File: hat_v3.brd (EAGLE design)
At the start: 65 x 56.5 mm, 25 parts, among them U1 ADS1115IDGST, U2 ADXL345

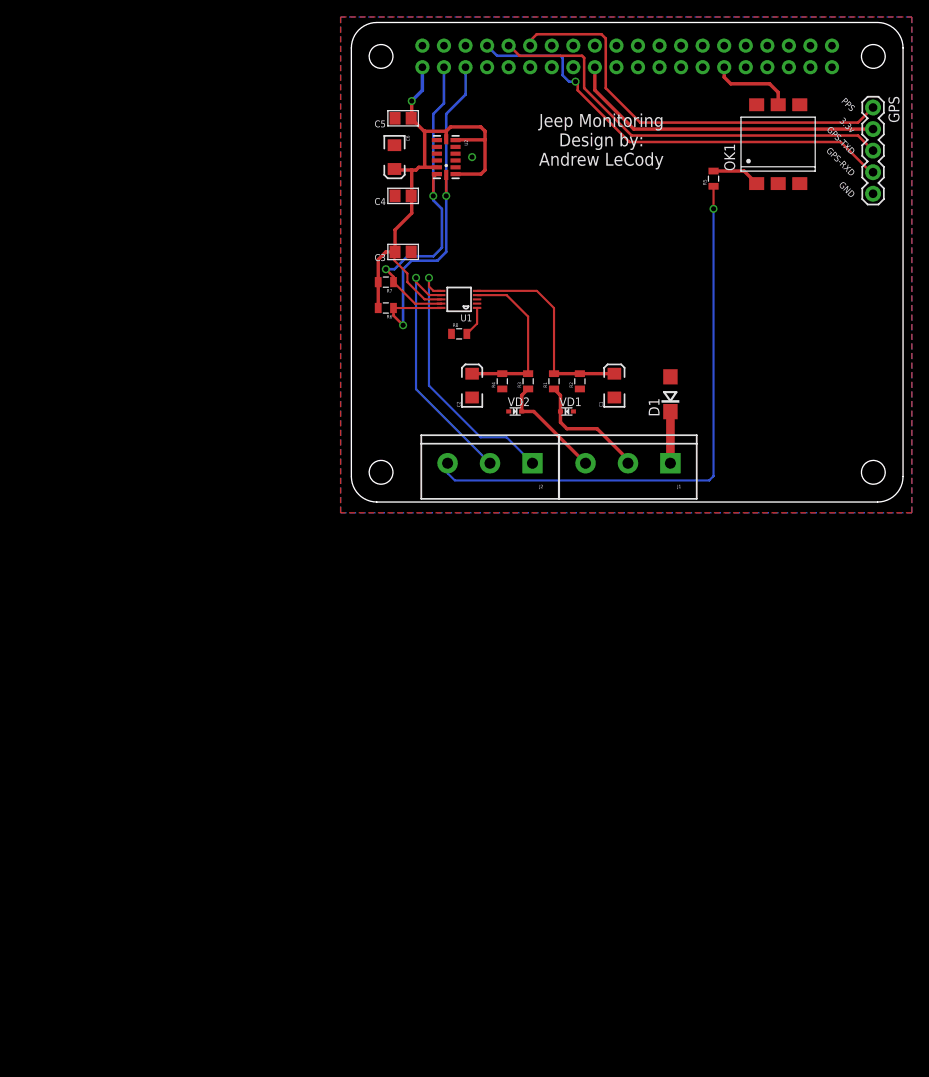
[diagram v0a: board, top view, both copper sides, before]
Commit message: V3 almost done, just need to finish MCP2515
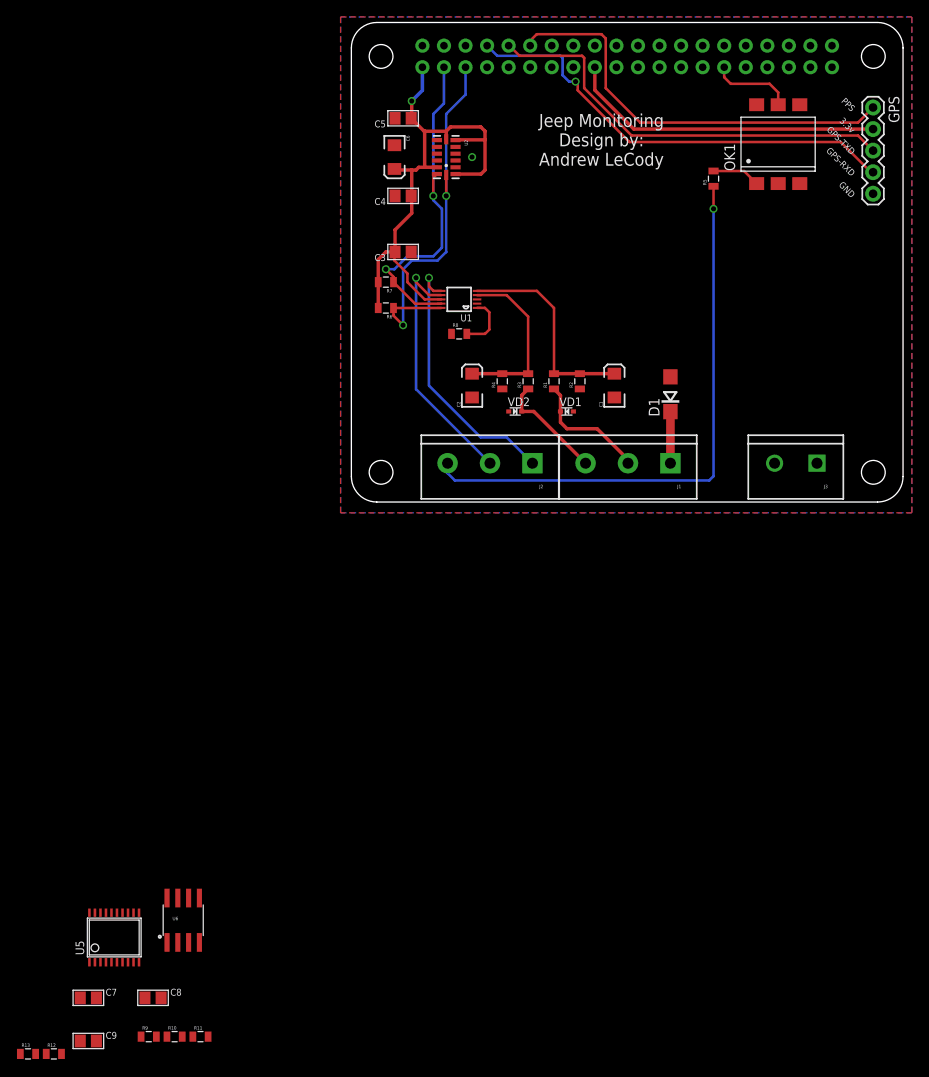
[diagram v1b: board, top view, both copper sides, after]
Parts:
- added C7, C8: 560pF, microbuilder:0805
- added C9: 0.1µF, microbuilder:0805
- added FRAME2: FRAME-LETTERNO_PACKAGE, SparkFun-Aesthetics:DUMMY
- added J3: (no value), SparkFun-Connectors:SCREWTERMINAL-5MM-2
- added R10, R11: 100, SparkFun-Passives:0805
- added R12: 10k, SparkFun-Passives:0805
- added R13: 22k, SparkFun-Passives:0805
- added R9: 4k7, SparkFun-Passives:0805
- added U5: MCP2515-I/ST, mcp2515:TSSOP20
- added U6: MCP2551, SparkFun-DigitalIC:SO08
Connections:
- removed net 5.0V: RPI1.2, RPI1.4
- new net 5V: C9.1, RPI1.2, RPI1.4, U6.2
- new net CANH: J3.1, R10.2, U6.7
- new net CANL: J3.2, R11.2, U6.6
- new net N$4: R12.1, R13.2, U5.2
- new net N$5: R9.2, U6.8
- new net N$6: C7.1, R10.1
- new net N$8: C8.1, R11.1
- new net RXCAN: R12.2, U6.4
- new net TXCAN: U5.1, U6.1
- new net VDD: U5.20
- new net VSS: U5.10
- net GND: now also C7.2, C8.2, C9.2, R13.1, R9.1, U6.3
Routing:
- net ADDR: track 3.57 -> 6.56 mm

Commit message: V3 done!
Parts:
- added C10: 100nF, microbuilder:0805
- added C11, C12: 22pF, microbuilder:0805
- added R14: 4k7, SparkFun-Passives:0805
- added X1: 16Mhz, IQD-Frequency-Products:HC49-4-HSMX
- U5: value MCP2515-I/ST -> MCP2515-I/SO; device mcp2515:TSSOP20 -> mcp2515:SO18L
- moved C9 114.0 mm to (45.7, 20.8), turned to 90 degrees
- moved R9 113.9 mm to (55.4, 18.8), turned to 270 degrees
- moved C7 112.5 mm to (54.9, 14.2)
- moved R13 107.6 mm to (27.4, 20.3), turned to 90 degrees
- moved R12 107.3 mm to (30.0, 20.3), turned to 270 degrees
- moved R10 104.2 mm to (52.8, 10.7), turned to 180 degrees
- moved C8 101.0 mm to (46.7, 14.2), turned to 180 degrees
- moved U5 99.5 mm to (24.9, 33.0), turned to 90 degrees
- moved U6 99.5 mm to (50.8, 20.8), turned to 180 degrees
- moved R11 99.3 mm to (48.8, 10.7)
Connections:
- removed net VDD: U5.20
- removed net VSS: U5.10
- new net N$14: C12.1, U5.8, X1.2
- new net N$15: C11.1, U5.7, X1.1
- new net U5_RST: R14.1, U5.17
- net 3.3V: now also C10.1, R14.2, U5.18
- net GND: now also C10.2, C11.2, C12.2, U5.9
- net GPIO25: now also U5.12
- net SPI_CE0: now also U5.16
- net SPI_MISO: now also U5.15
- net SPI_MOSI: now also U5.14
- net SPI_SCLK: now also U5.13
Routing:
- net 5V: track 0.00 -> 128.1 mm, vias 0 -> 1
- net TXCAN: track 0.00 -> 37.1 mm
- net SPI_CE0: track 0.00 -> 35.5 mm, vias 0 -> 1
- net SPI_MISO: track 0.00 -> 31.3 mm, vias 0 -> 2
- net SPI_MOSI: track 0.00 -> 29.0 mm, vias 0 -> 2
- net SPI_SCLK: track 0.00 -> 26.9 mm, vias 0 -> 1
- net GPIO25: track 0.00 -> 26.8 mm, vias 0 -> 1
- net RXCAN: track 0.00 -> 20.7 mm
- net N$15: track 0.00 -> 18.4 mm
- net CANH: track 0.00 -> 15.1 mm
- net CANL: track 0.00 -> 13.9 mm
- net 3.3V: track 103.6 -> 117.5 mm
- net N$14: track 0.00 -> 12.8 mm
- net N$4: track 0.00 -> 12.8 mm
- net N$5: track 0.00 -> 5.59 mm
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
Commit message: Reworked v3
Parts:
- removed R13: 22k, SparkFun-Passives:0805
- removed R14: 4k7, SparkFun-Passives:0805
- removed U6: MCP2551, SparkFun-DigitalIC:SO08
- added D2: (no value), diode:SOT23
- added U4: MCP2551, SparkFun-DigitalIC:SO08
- C1, C2: value 100uF -> 10uF; device SparkFun:EIA3216 -> SparkFun-Capacitors:EIA3216
- C10: value 100nF -> 0.1uF
- C6: device SparkFun:EIA3216 -> SparkFun-Capacitors:EIA3216
- R10: value 100 -> 10k
- R11: value 100 -> 22k
- R12, R7: value 10k -> 4k7
- R8: value 10k -> 100
- R9: value 4k7 -> 100
- VD1, VD2: device diode:SOD523@1 -> diode:SOD523
- moved R7 51.7 mm to (55.4, 19.3), turned to 270 degrees
- moved R8 41.1 mm to (52.8, 11.2), turned to 180 degrees
- moved R10 24.8 mm to (30.0, 20.3), turned to 270 degrees
- moved R11 23.4 mm to (27.4, 20.3), turned to 90 degrees
- moved R12 20.8 mm to (15.2, 35.1)
- moved VD1 16.8 mm to (8.64, 11.7)
- moved VD2 14.8 mm to (4.57, 11.7), turned to 0 degrees
- moved R9 10.1 mm to (48.8, 11.2), turned to 0 degrees
- moved R6 9.16 mm to (12.7, 19.8), turned to 0 degrees
- moved R1 3.56 mm to (23.9, 17.8)
- moved R3 3.56 mm to (20.8, 17.8)
- moved C3 3.41 mm to (4.57, 26.4), turned to 270 degrees
- moved C10 2.96 mm to (15.2, 30.5), turned to 270 degrees
- moved D1 1.02 mm to (37.6, 13.7)
- moved C1 0.51 mm to (31.0, 14.2)
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- renumbered U5 to U3
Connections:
- net 3.3V: now also R12.2; no longer R14.2, R6.2, R7.2
- net 5V: now also U4.2; no longer U6.2
- net ADDR: now also R6.2; no longer R8.2
- net BAT-1-INPUT: now also D2.1; no longer VD1.C
- net BAT-2-INPUT: now also D2.2; no longer VD2.C
- net CANH: now also R8.2, U4.7; no longer R10.2, U6.7
- net CANL: now also R9.2, U4.6; no longer R11.2, U6.6
- net GND: now also D2.3, R11.1, R6.1, R7.1, U4.3; no longer R13.1, R8.1, R9.1, U6.3
- net N$4: now also R10.1, R11.2; no longer R12.1, R13.2
- net N$5: now also R7.2, U4.8; no longer R9.2, U6.8
- net N$6: now also R8.1; no longer R10.1
- net N$8: now also R9.1; no longer R11.1
- net RXCAN: now also R10.2, U4.4; no longer R12.2, U6.4
- net SCL: no longer R6.1
- net SDA: no longer R7.1
- net SHUNT-HIGH-INPUT: now also VD1.C
- net SHUNT-LOW-INPUT: now also VD2.C
- net TXCAN: now also U4.1; no longer U6.1
- net U5_RST: now also R12.1; no longer R14.1
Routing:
- net 3.3V: track 117.5 -> 138.4 mm, vias 1 -> 0
- net GND: track 0.00 -> 16.6 mm, vias 8 -> 17
- net SHUNT-LOW-INPUT: track 29.6 -> 42.8 mm, vias 1 -> 2
- net SDA: track 40.5 -> 49.9 mm
- net SHUNT-HIGH-INPUT: track 33.1 -> 41.1 mm, vias 1 -> 2
- net U5_RST: track 4.61 -> 11.1 mm
- net BAT-2-INPUT: track 13.0 -> 17.4 mm, vias 0 -> 1
- net SCL: track 45.8 -> 49.4 mm
- net BAT-1-INPUT: track 14.4 -> 17.3 mm, vias 0 -> 1
- net GPIO25: track 26.8 -> 28.6 mm
- net SPI_SCLK: track 26.9 -> 28.1 mm
- net N$1: track 6.08 -> 7.09 mm
- net BAT-2: track 20.4 -> 19.5 mm
- net BAT-1: track 24.7 -> 23.8 mm
- net SPI_MOSI: track 29.0 -> 29.5 mm
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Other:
- board text added: "Bat 1"
- board text added: "Bat 2"
- board text added: "CANH"
- board text added: "CANL"
- board text added: "High"
- board text added: "Link"
- board text added: "Low"
- board text added: "RXD-I"
- board text added: "TXD-I"
- board text removed: "GPS-RXD"
- board text removed: "GPS-TXD"

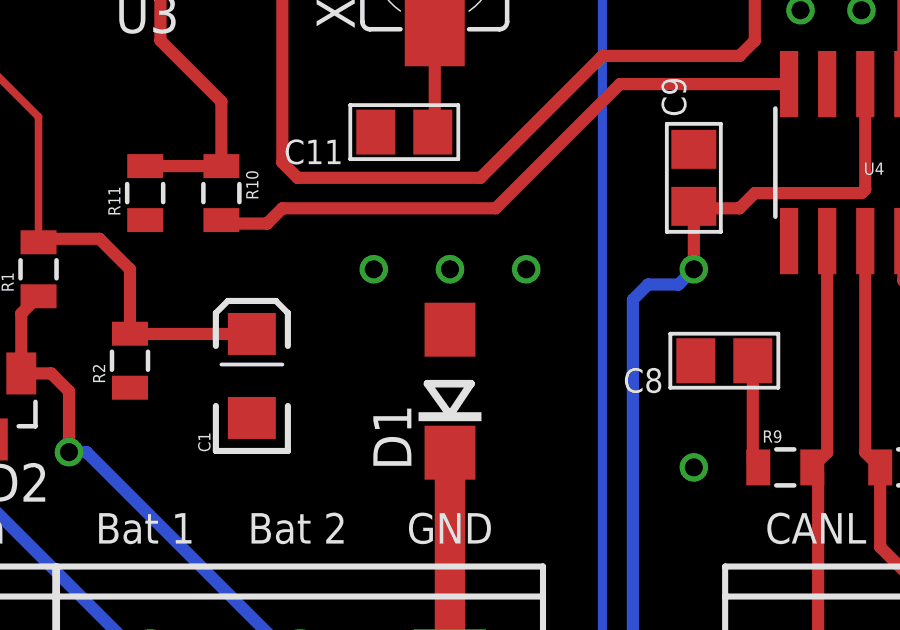
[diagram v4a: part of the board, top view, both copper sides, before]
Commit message: Tweaked placement of a via for ground
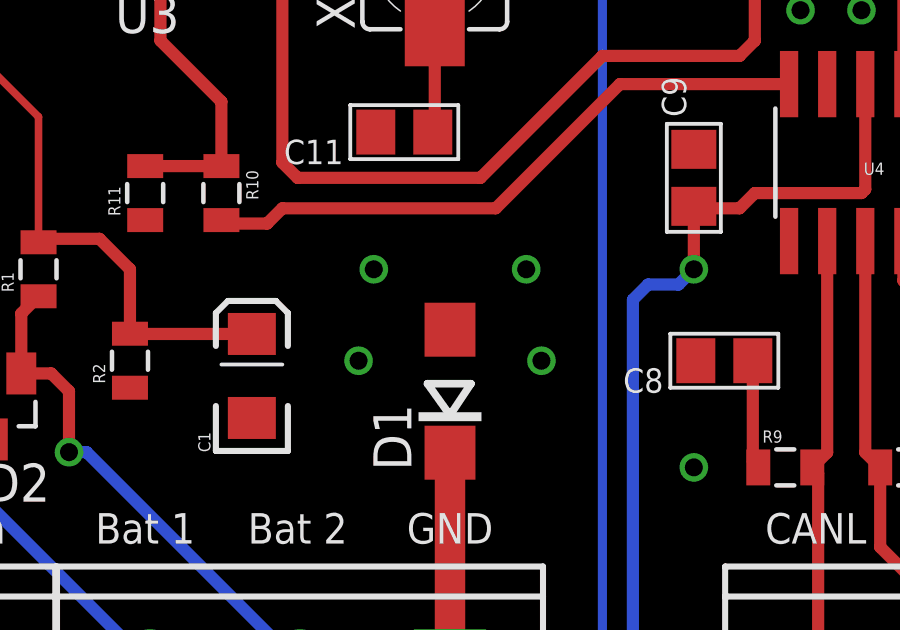
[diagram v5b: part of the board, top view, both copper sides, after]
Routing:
- net GND: vias 17 -> 18
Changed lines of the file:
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@@
 <via x="40.132" y="17.78" extent="1-16" drill="0.6" shape="square"/>
 <via x="35.052" y="17.78" extent="1-16" drill="0.6" shape="square"/>
-<via x="37.592" y="17.78" extent="1-16" drill="0.6" shape="square"/>
+<via x="34.544" y="14.732" extent="1-16" drill="0.6" shape="square"/>
 <contactref element="D2" pad="3"/>
 <wire x1="14.8131" y1="23.876" x2="16.764" y2="23.876" width="0.254" layer="1"/>
@@
 <via x="45.72" y="11.176" extent="1-16" drill="0.6" shape="square"/>
 <via x="55.88" y="11.176" extent="1-16" drill="0.6" shape="square"/>
+<via x="40.64" y="14.732" extent="1-16" drill="0.6" shape="square"/>
 </signal>
 <signal name="TXD">
